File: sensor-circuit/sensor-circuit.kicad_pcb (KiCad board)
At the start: 2 copper layers, 70 x 70 mm, 50 parts

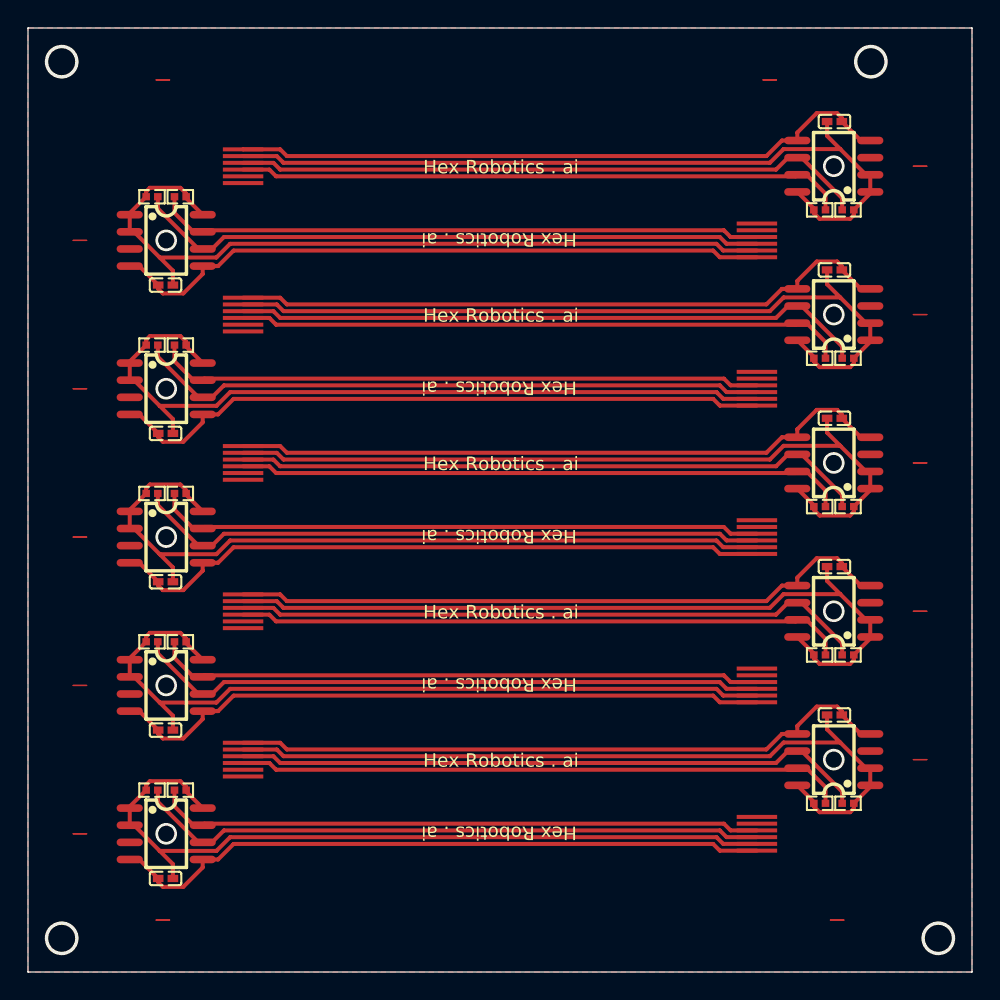
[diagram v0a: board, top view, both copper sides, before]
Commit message: Finish the control circuit layout.
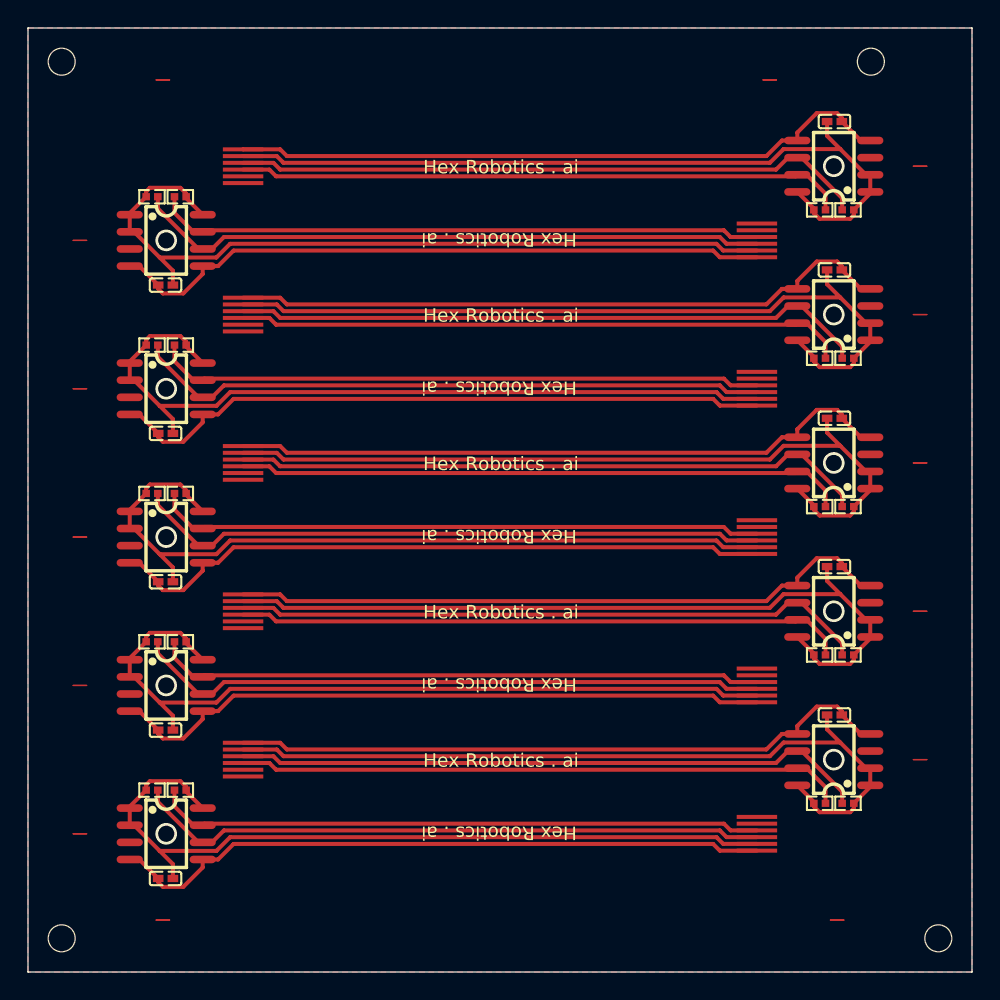
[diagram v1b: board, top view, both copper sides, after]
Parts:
- added REF**: NPTH 2mm hole 3mm clearence, Library:NPTH 2mm hole 3mm clearence, F.Cu at (202.8, 42.2)
- added REF**: NPTH 2mm hole 3mm clearence, Library:NPTH 2mm hole 3mm clearence, F.Cu at (142.8, 107.2)
- added REF**: NPTH 2mm hole 3mm clearence, Library:NPTH 2mm hole 3mm clearence, F.Cu at (142.8, 42.2)
- added REF**: NPTH 2mm hole 3mm clearence, Library:NPTH 2mm hole 3mm clearence, F.Cu at (207.8, 107.2)
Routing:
- net (no net): vias 14 -> 10

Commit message: Fix sensors panel for production.
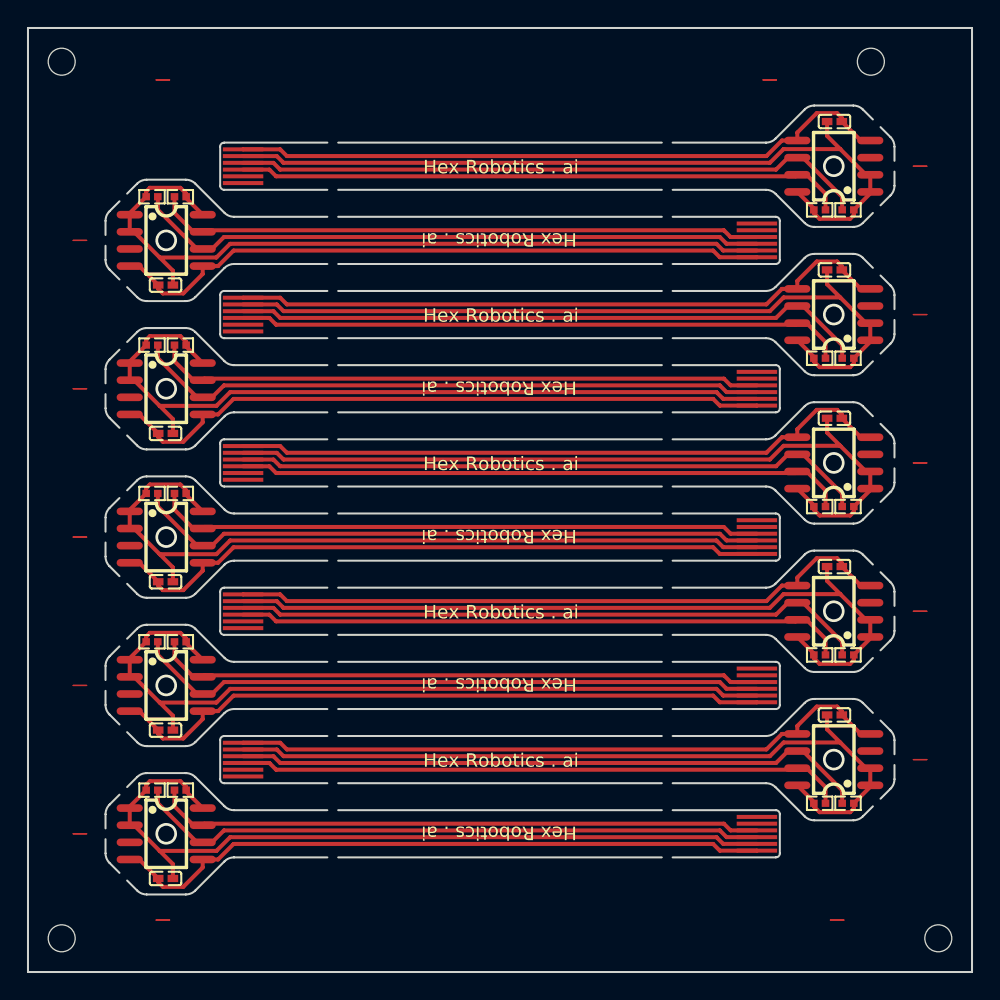
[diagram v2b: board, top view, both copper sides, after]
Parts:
- removed the C1 at (150.5, 80.8)
- removed the C1 at (200.0, 57.7)
- removed the C1 at (150.5, 69.8)
- removed the C1 at (200.0, 79.7)
- removed the C1 at (150.5, 58.8)
- removed the C1 at (150.5, 91.8)
- removed the C1 at (150.5, 102.8)
- removed the C1 at (200.0, 90.7)
- removed the C1 at (200.0, 68.7)
- removed the FPC1 at (194.3, 55.5)
- removed the FPC1 at (156.2, 94.0)
- removed the FPC1 at (156.2, 61.0)
- removed the FPC1 at (194.3, 77.5)
- removed the FPC1 at (156.2, 83.0)
- removed the FPC1 at (194.3, 88.5)
- removed the FPC1 at (194.3, 99.5)
- removed the FPC1 at (156.2, 72.0)
- removed the FPC1 at (194.3, 66.5)
- removed the R1 at (151.5, 74.3)
- removed the R1 at (199.0, 75.2)
- removed the R1 at (151.5, 85.3)
- removed the R1 at (151.5, 63.3)
- removed the R1 at (199.0, 86.2)
- removed the R1 at (151.5, 96.3)
- removed the R1 at (199.0, 97.2)
- removed the R1 at (199.0, 64.2)
- removed the R1 at (151.5, 52.3)
- removed the R2 at (149.4, 85.3)
- removed the R2 at (149.4, 63.3)
- removed the R2 at (149.4, 96.3)
- removed the R2 at (201.1, 97.2)
- removed the R2 at (201.1, 86.2)
- removed the R2 at (149.4, 74.3)
- removed the R2 at (149.4, 52.3)
- removed the R2 at (201.1, 75.2)
- removed the R2 at (201.1, 64.2)
- removed the U1 at (150.5, 88.5)
- removed the U1 at (150.5, 77.5)
- removed the U1 at (150.5, 99.5)
- removed the U1 at (200.0, 72.0)
- removed the U1 at (200.0, 94.0)
- removed the U1 at (200.0, 61.0)
- removed the U1 at (150.5, 55.5)
- removed the U1 at (200.0, 83.0)
- removed the U1 at (150.5, 66.5)
- added C10: 100nF, Library:C0402, F.Cu at (150.5, 91.8)
- added C2: 100nF, Library:C0402, F.Cu at (200.0, 90.7)
- added C3: 100nF, Library:C0402, F.Cu at (150.5, 69.8)
- added C4: 100nF, Library:C0402, F.Cu at (200.0, 79.7)
- added C5: 100nF, Library:C0402, F.Cu at (150.5, 80.8)
- added C6: 100nF, Library:C0402, F.Cu at (200.0, 68.7)
- added C7: 100nF, Library:C0402, F.Cu at (150.5, 102.8)
- added C8: 100nF, Library:C0402, F.Cu at (150.5, 58.8)
- added C9: 100nF, Library:C0402, F.Cu at (200.0, 57.7)
- added FPC10: ~, Library:FPC-6P-P0.50-Pattern, F.Cu at (194.3, 88.5)
- added FPC2: ~, Library:FPC-6P-P0.50-Pattern, F.Cu at (156.2, 94.0)
- added FPC3: ~, Library:FPC-6P-P0.50-Pattern, F.Cu at (194.3, 66.5)
- added FPC4: ~, Library:FPC-6P-P0.50-Pattern, F.Cu at (156.2, 83.0)
- added FPC5: ~, Library:FPC-6P-P0.50-Pattern, F.Cu at (194.3, 77.5)
- added FPC6: ~, Library:FPC-6P-P0.50-Pattern, F.Cu at (156.2, 72.0)
- added FPC7: ~, Library:FPC-6P-P0.50-Pattern, F.Cu at (194.3, 99.5)
- added FPC8: ~, Library:FPC-6P-P0.50-Pattern, F.Cu at (194.3, 55.5)
- added FPC9: ~, Library:FPC-6P-P0.50-Pattern, F.Cu at (156.2, 61.0)
- added R10: 10kΩ, Library:R0402, F.Cu at (149.4, 74.3)
- added R11: 10kΩ, Library:R0402, F.Cu at (199.0, 75.2)
- added R12: 10kΩ, Library:R0402, F.Cu at (201.1, 75.2)
- added R13: 10kΩ, Library:R0402, F.Cu at (151.5, 96.3)
- added R14: 10kΩ, Library:R0402, F.Cu at (149.4, 96.3)
- added R15: 10kΩ, Library:R0402, F.Cu at (151.5, 52.3)
- added R16: 10kΩ, Library:R0402, F.Cu at (149.4, 52.3)
- added R17: 10kΩ, Library:R0402, F.Cu at (199.0, 64.2)
- added R18: 10kΩ, Library:R0402, F.Cu at (201.1, 64.2)
- added R19: 10kΩ, Library:R0402, F.Cu at (151.5, 85.3)
- added R20: 10kΩ, Library:R0402, F.Cu at (149.4, 85.3)
- added R3: 10kΩ, Library:R0402, F.Cu at (199.0, 97.2)
- added R4: 10kΩ, Library:R0402, F.Cu at (201.1, 97.2)
- added R5: 10kΩ, Library:R0402, F.Cu at (151.5, 63.3)
- added R6: 10kΩ, Library:R0402, F.Cu at (149.4, 63.3)
- added R7: 10kΩ, Library:R0402, F.Cu at (199.0, 86.2)
- added R8: 10kΩ, Library:R0402, F.Cu at (201.1, 86.2)
- added R9: 10kΩ, Library:R0402, F.Cu at (151.5, 74.3)
- added U10: ~, Library:SOIC-8_L5.0-W4.0-P1.27-LS6.0-BL, F.Cu at (150.5, 88.5)
- added U2: ~, Library:SOIC-8_L5.0-W4.0-P1.27-LS6.0-BL, F.Cu at (200.0, 94.0)
- added U3: ~, Library:SOIC-8_L5.0-W4.0-P1.27-LS6.0-BL, F.Cu at (150.5, 66.5)
- added U4: ~, Library:SOIC-8_L5.0-W4.0-P1.27-LS6.0-BL, F.Cu at (200.0, 83.0)
- added U5: ~, Library:SOIC-8_L5.0-W4.0-P1.27-LS6.0-BL, F.Cu at (150.5, 77.5)
- added U6: ~, Library:SOIC-8_L5.0-W4.0-P1.27-LS6.0-BL, F.Cu at (200.0, 72.0)
- added U7: ~, Library:SOIC-8_L5.0-W4.0-P1.27-LS6.0-BL, F.Cu at (150.5, 99.5)
- added U8: ~, Library:SOIC-8_L5.0-W4.0-P1.27-LS6.0-BL, F.Cu at (150.5, 55.5)
- added U9: ~, Library:SOIC-8_L5.0-W4.0-P1.27-LS6.0-BL, F.Cu at (200.0, 61.0)
- turned U1 to 180 degrees
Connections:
- net 3V3 renamed /sensor-circuit-singlet/3V3
- net GND renamed /sensor-circuit-singlet/GND
- net SCL renamed /sensor-circuit-singlet/SCL
- net SDA renamed /sensor-circuit-singlet/SDA
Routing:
- net /sensor-circuit-singlet/3V3: track 592.0 -> 59.2 mm
- net /sensor-circuit-singlet/GND: track 493.8 -> 49.4 mm
- net /sensor-circuit-singlet/SDA: track 471.1 -> 47.2 mm
- net /sensor-circuit-singlet/SCL: track 452.2 -> 45.2 mm
- net /sensor-circuit-singlet4/3V3: track 0.00 -> 59.2 mm
- net /sensor-circuit-singlet9/3V3: track 0.00 -> 59.2 mm
- net /sensor-circuit-singlet6/3V3: track 0.00 -> 59.2 mm
- net /sensor-circuit-singlet5/3V3: track 0.00 -> 59.2 mm
- net /sensor-circuit-singlet3/3V3: track 0.00 -> 59.2 mm
- net /sensor-circuit-singlet1/3V3: track 0.00 -> 59.2 mm
- net /sensor-circuit-singlet8/3V3: track 0.00 -> 59.2 mm
- net /sensor-circuit-singlet2/3V3: track 0.00 -> 59.2 mm
- net /sensor-circuit-singlet7/3V3: track 0.00 -> 59.2 mm
- net /sensor-circuit-singlet9/GND: track 0.00 -> 49.4 mm
- net /sensor-circuit-singlet6/GND: track 0.00 -> 49.4 mm
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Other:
- outline, holes or cut-outs redrawn
